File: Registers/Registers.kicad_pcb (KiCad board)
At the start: 2 copper layers, 85 x 99.5 mm, 19 parts

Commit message: Some small Changes
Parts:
- added C1: 100 nF, Capacitor_THT:C_Disc_D5.0mm_W2.5mm_P2.50mm, F.Cu at (92.7, 42.2)
- added C2: 100 nF, Capacitor_THT:C_Disc_D5.0mm_W2.5mm_P2.50mm, F.Cu at (82.8, 118.5)
- added C3: 100 nF, Capacitor_THT:C_Disc_D5.0mm_W2.5mm_P2.50mm, F.Cu at (84.0, 110.0)
- added C4: 100 nF, Capacitor_THT:C_Disc_D5.0mm_W2.5mm_P2.50mm, F.Cu at (45.5, 90.0)
- added J1: Output to Display, Connector_PinHeader_2.54mm:PinHeader_1x04_P2.54mm_Vertical, F.Cu at (68.1, 124.5)
- added J2: Reg Specific Connections, Connector_PinSocket_2.54mm:PinSocket_1x10_P2.54mm_Vertical, F.Cu at (76.0, 45.0)
- added U1: 74HC173, Package_DIP:DIP-16_W7.62mm_Socket_LongPads, F.Cu at (42.4, 81.1)
- added U2: 74HC173, Package_DIP:DIP-16_W7.62mm_Socket_LongPads, F.Cu at (73.9, 81.1)
- added U3: 74HC245, Package_DIP:DIP-20_W7.62mm_Socket_LongPads, F.Cu at (39.9, 63.1)
- added U4: ATtiny84-20P, Package_DIP:DIP-14_W7.62mm, F.Cu at (36.0, 98.5)
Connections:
- B1 pad 10: BUS7 -> BUS0
- B1 pad 11: LBA0 -> LBA7
- B1 pad 12: LBA1 -> LBA6
- B1 pad 13: LBA2 -> LBA5
- B1 pad 14: LBA3 -> LBA4
- B1 pad 15: LBA4 -> LBA3
- B1 pad 16: LBA5 -> LBA2
- B1 pad 17: LBA6 -> LBA1
- B1 pad 18: LBA7 -> LBA0
- B1 pad 19: LBB0 -> LBB7
- B1 pad 20: LBB1 -> LBB6
- B1 pad 21: LBB2 -> LBB5
- B1 pad 22: LBB3 -> LBB4
- B1 pad 23: LBB4 -> LBB3
- B1 pad 24: LBB5 -> LBB2
- B1 pad 25: LBB6 -> LBB1
- B1 pad 26: LBB7 -> LBB0
- B1 pad 3: BUS0 -> BUS7
- B1 pad 4: BUS1 -> BUS6
- B1 pad 5: BUS2 -> BUS5
- B1 pad 6: BUS3 -> BUS4
- B1 pad 7: BUS4 -> BUS3
- B1 pad 8: BUS5 -> BUS2
- B1 pad 9: BUS6 -> BUS1
- B2 pad 10: BUS7 -> BUS0
- B2 pad 3: BUS0 -> BUS7
- B2 pad 4: BUS1 -> BUS6
- B2 pad 5: BUS2 -> BUS5
- B2 pad 6: BUS3 -> BUS4
- B2 pad 7: BUS4 -> BUS3
- B2 pad 8: BUS5 -> BUS2
- B2 pad 9: BUS6 -> BUS1
- D1 pad 2: unconnected-(D1-A-Pad2) -> REG0
- D2 pad 2: unconnected-(D2-A-Pad2) -> REG1
- D3 pad 2: unconnected-(D3-A-Pad2) -> REG2
- D4 pad 2: unconnected-(D4-A-Pad2) -> REG3
- D5 pad 2: unconnected-(D5-A-Pad2) -> REG4
- D6 pad 2: unconnected-(D6-A-Pad2) -> REG5
- D7 pad 2: unconnected-(D7-A-Pad2) -> REG6
- D8 pad 2: unconnected-(D8-A-Pad2) -> REG7
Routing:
- net 5V: track 9.15 -> 43.0 mm
- net CLEAR: track 3.90 -> 35.3 mm, vias 0 -> 1
- net GND: track 45.3 -> 75.9 mm
- net LBB5: track 3.90 -> 16.3 mm
- net LBA5: track 3.90 -> 15.6 mm
- net LBA4: track 3.90 -> 13.5 mm
- net LBB4: track 3.90 -> 13.5 mm
- net CTRL-27: track 4.12 -> 11.7 mm
- net LBB3: track 3.90 -> 8.59 mm
- net LBA3: track 3.90 -> 8.59 mm
- net RAMI: track 3.80 -> 8.06 mm
- net CTRL-31: track 3.80 -> 8.06 mm
- net CTRL-26: track 3.80 -> 8.06 mm
- net CTRL-24: track 3.80 -> 8.06 mm
- net CTRL-19: track 3.80 -> 8.06 mm
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
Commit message: Version of Registers PCB that is before routing.
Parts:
- added J3: LED Wire Bus, Connector_PinSocket_2.54mm:PinSocket_1x08_P2.54mm_Vertical, F.Cu at (76.1, 40.0)
- added J4: LED Wire Bus, Connector_PinSocket_2.54mm:PinSocket_1x08_P2.54mm_Vertical, F.Cu at (84.0, 68.5)
- moved C1 71.0 mm to (38.2, 87.8), turned to 90 degrees
- moved C3 48.8 mm to (51.0, 74.0), turned to 180 degrees
- moved C2 33.3 mm to (71.0, 87.4), turned to 90 degrees
- moved J2 26.6 mm to (67.5, 70.2), turned to 180 degrees
- moved U3 15.7 mm to (54.1, 69.7), turned to 180 degrees
- moved U1 9.57 mm to (45.7, 90.1)
- moved U2 9.10 mm to (75.9, 90.0)
- moved C4 7.62 mm to (44.2, 97.5)
- moved U4 5.43 mm to (39.2, 102.9)
- moved J1 1.62 mm to (68.7, 123.0)
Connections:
- D1 pad 2: REG0 -> Net-(D1-A)
- D2 pad 2: REG1 -> Net-(D2-A)
- D3 pad 2: REG2 -> Net-(D3-A)
- D4 pad 2: REG3 -> Net-(D4-A)
- D5 pad 2: REG4 -> Net-(D5-A)
- D6 pad 2: REG5 -> Net-(D6-A)
- D7 pad 2: REG6 -> Net-(D7-A)
- D8 pad 2: REG7 -> Net-(D8-A)
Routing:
- net 5V: track 43.0 -> 9.15 mm
- net CLEAR: track 35.3 -> 3.90 mm, vias 1 -> 0
- net GND: track 75.9 -> 45.3 mm
- net LBB5: track 16.3 -> 3.90 mm
- net LBA5: track 15.6 -> 3.90 mm
- net LBA4: track 13.5 -> 3.90 mm
- net LBB4: track 13.5 -> 3.90 mm
- net CTRL-27: track 11.7 -> 4.12 mm
- net LBB3: track 8.59 -> 3.90 mm
- net LBA3: track 8.59 -> 3.90 mm
- net RAMI: track 8.06 -> 3.80 mm
- net CTRL-31: track 8.06 -> 3.80 mm
- net CTRL-26: track 8.06 -> 3.80 mm
- net CTRL-24: track 8.06 -> 3.80 mm
- net CTRL-19: track 8.06 -> 3.80 mm
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
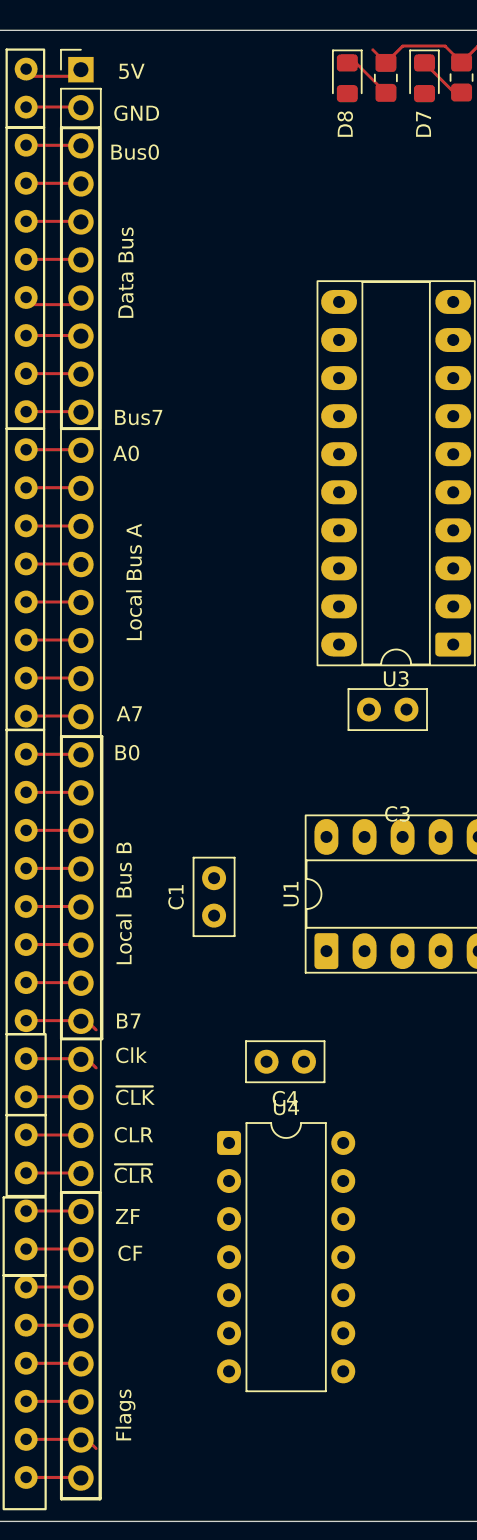
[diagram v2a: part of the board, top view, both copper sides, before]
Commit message: Fixed some issues with the orientation of the local buses on the side-rails.
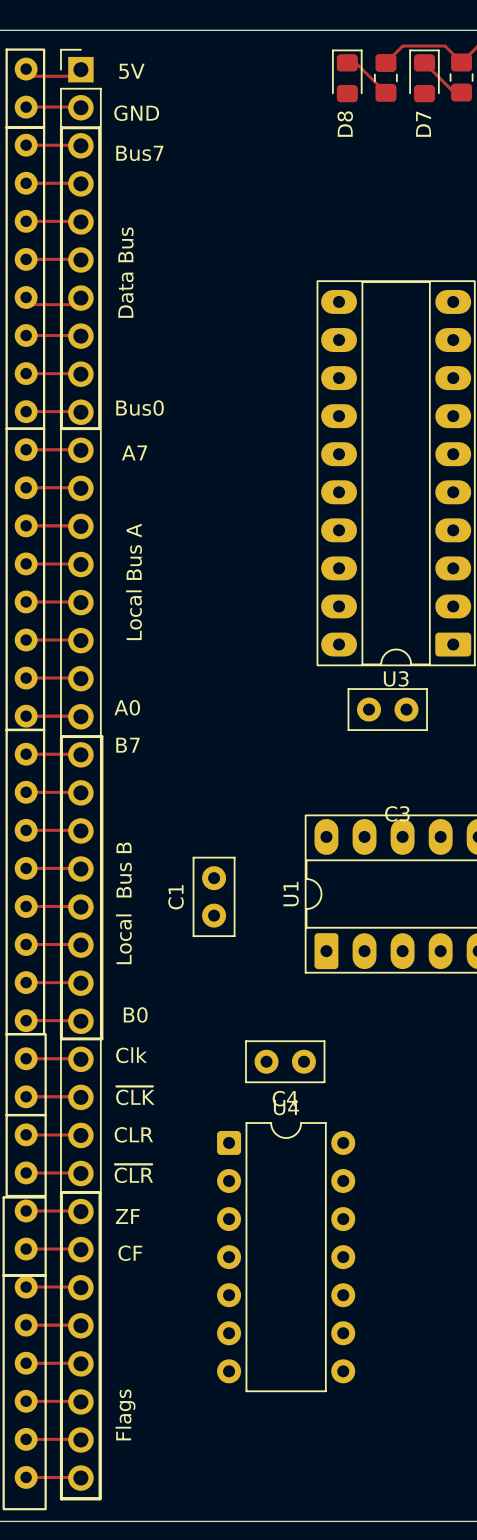
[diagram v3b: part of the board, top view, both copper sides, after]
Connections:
- B2 pad 11: LBA0 -> LBA7
- B2 pad 12: LBA1 -> LBA6
- B2 pad 13: LBA2 -> LBA5
- B2 pad 14: LBA3 -> LBA4
- B2 pad 15: LBA4 -> LBA3
- B2 pad 16: LBA5 -> LBA2
- B2 pad 17: LBA6 -> LBA1
- B2 pad 18: LBA7 -> LBA0
- B2 pad 19: LBB0 -> LBB7
- B2 pad 20: LBB1 -> LBB6
- B2 pad 21: LBB2 -> LBB5
- B2 pad 22: LBB3 -> LBB4
- B2 pad 23: LBB4 -> LBB3
- B2 pad 24: LBB5 -> LBB2
- B2 pad 25: LBB6 -> LBB1
- B2 pad 26: LBB7 -> LBB0
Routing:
- net GND: track 45.3 -> 44.0 mm

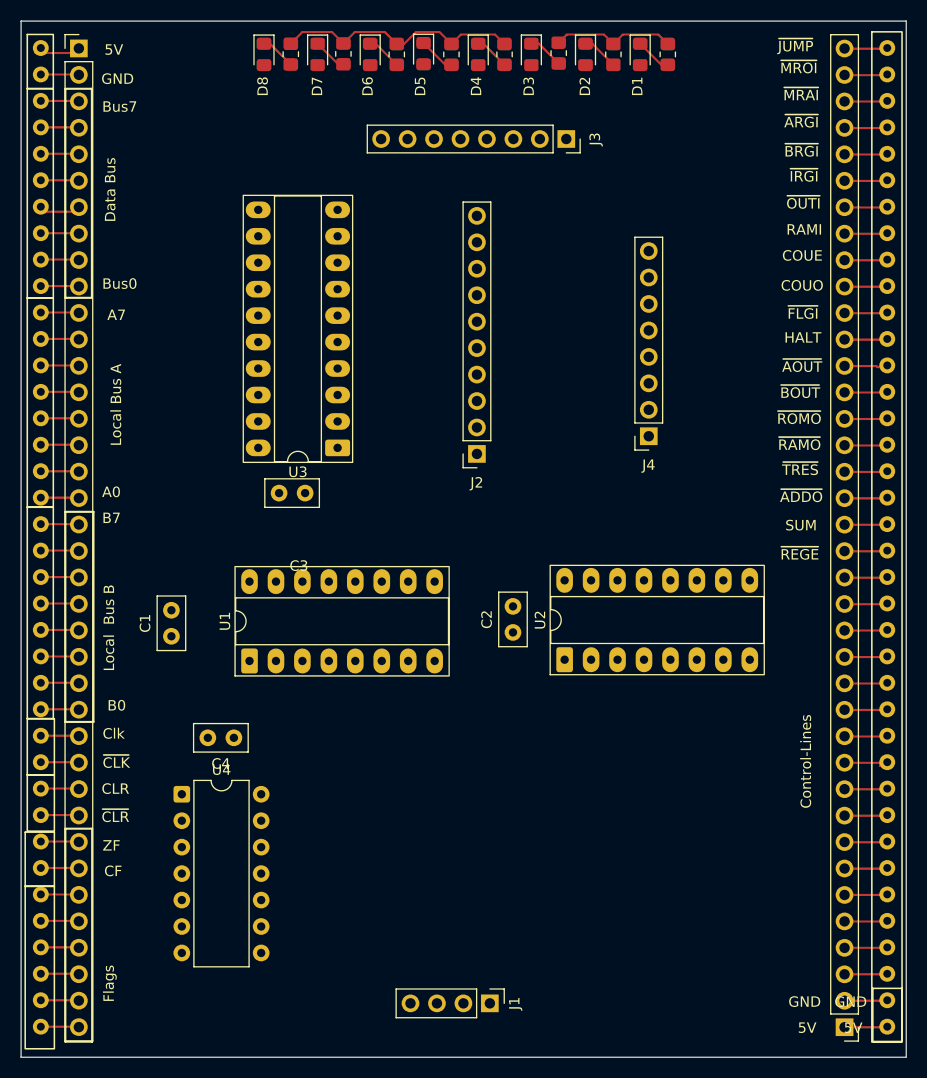
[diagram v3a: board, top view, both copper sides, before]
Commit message: Split 5V pins into different nets
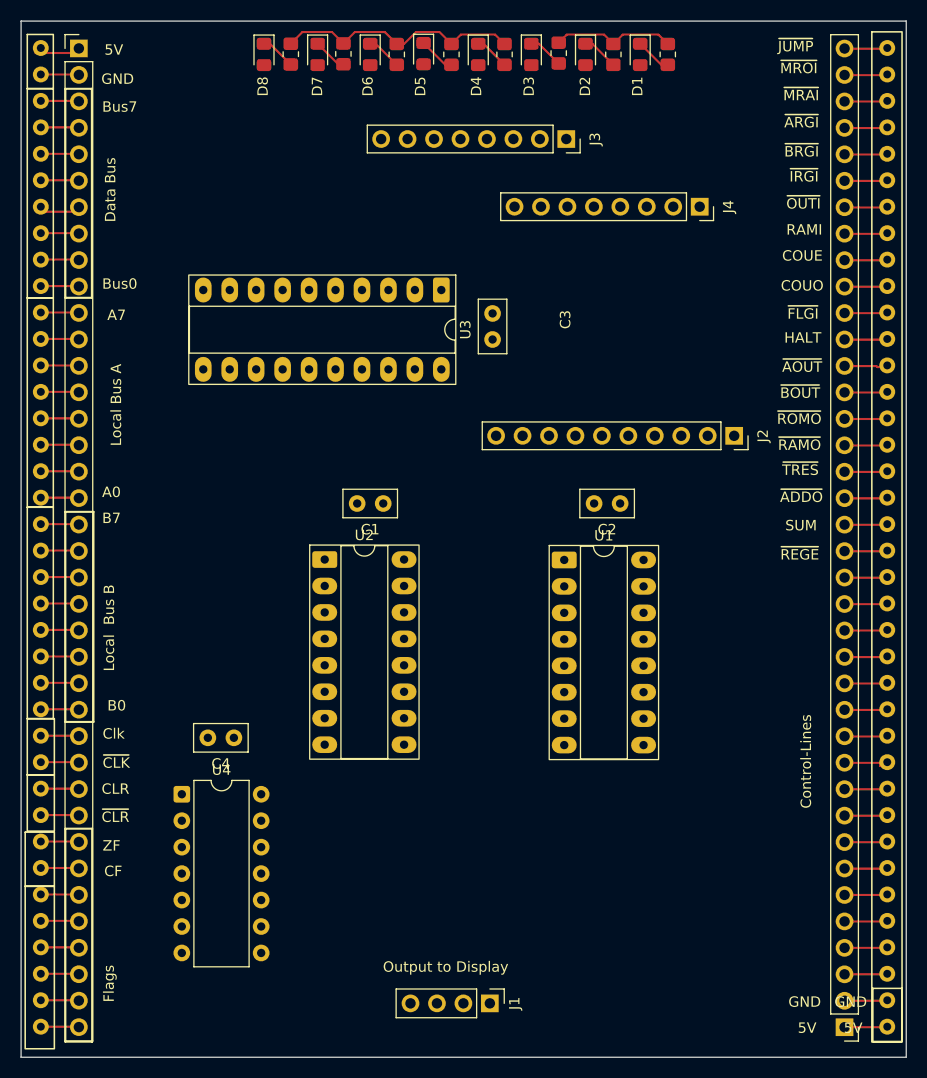
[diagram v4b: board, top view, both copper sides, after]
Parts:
- moved U1 31.7 mm to (75.9, 80.4), turned to 0 degrees
- moved U2 25.0 mm to (52.9, 80.4), turned to 0 degrees
- moved C3 24.9 mm to (69.0, 56.8), turned to -90 degrees
- moved J2 24.8 mm to (92.2, 68.5), turned to -90 degrees
- moved C1 24.0 mm to (58.5, 75.0), turned to 180 degrees
- moved J4 22.6 mm to (88.9, 46.5), turned to -90 degrees
- moved U3 18.1 mm to (64.1, 54.5), turned to -90 degrees
- moved C2 16.1 mm to (81.2, 75.0), turned to 180 degrees
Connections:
- B3 pad 1: 5V -> 5V_2
- C4 pad 2: 5V -> 5V_2
- J1 pad 1: 5V -> 5V_2
- U4 pad 1: 5V -> 5V_2

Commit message: First version of Registers
Routing done for PCB
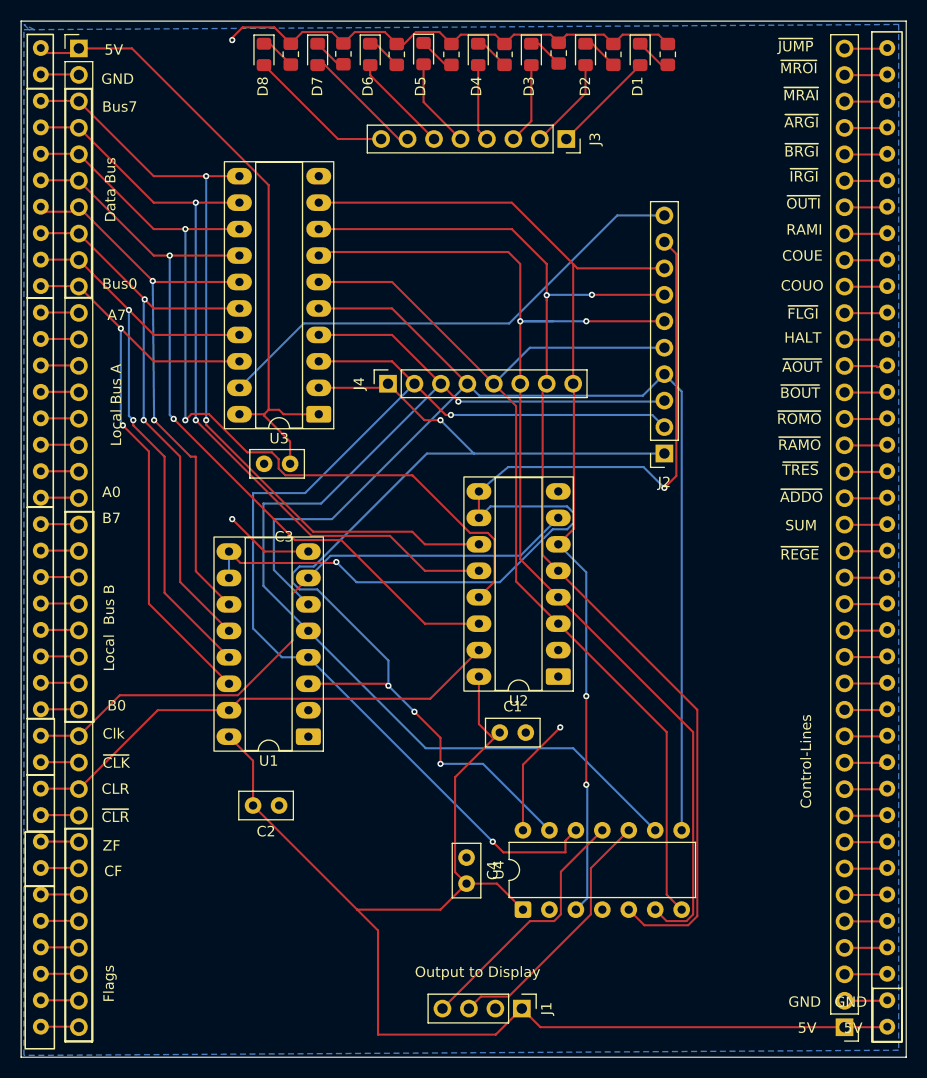
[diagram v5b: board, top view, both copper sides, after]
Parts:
- moved C2 43.7 mm to (48.5, 104.0)
- moved U4 34.6 mm to (71.9, 114.0), turned to 90 degrees
- moved J4 34.4 mm to (59.0, 63.5), turned to 90 degrees
- moved U1 29.9 mm to (51.3, 97.4), turned to 180 degrees
- moved C4 25.1 mm to (66.5, 109.0), turned to -90 degrees
- moved U2 25.1 mm to (75.3, 91.6), turned to 180 degrees
- moved C1 24.7 mm to (69.7, 97.0), turned to 0 degrees
- moved C3 24.2 mm to (49.6, 71.2), turned to 180 degrees
- moved U3 16.8 mm to (52.3, 66.4), turned to 180 degrees
- moved J2 6.91 mm to (85.5, 70.2), turned to 180 degrees
- moved J1 3.11 mm to (71.8, 123.5)
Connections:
- B1 pad 39: 5V -> 5V_2
- C1 pad 1: 5V -> 5V_2
- C2 pad 2: 5V -> 5V_2
- U1 pad 16: 5V -> 5V_2
- U2 pad 16: 5V -> 5V_2
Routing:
- net 5V_2: track 0.00 -> 126.5 mm
- net REG3: track 0.00 -> 115.5 mm
- net REG2: track 0.00 -> 113.0 mm, vias 0 -> 1
- net REG6: track 0.00 -> 111.6 mm, vias 0 -> 2
- net REG5: track 0.00 -> 110.6 mm, vias 0 -> 2
- net REG1: track 0.00 -> 110.1 mm, vias 0 -> 2
- net REG0: track 0.00 -> 103.8 mm, vias 0 -> 4
- net REG7: track 0.00 -> 100.1 mm, vias 0 -> 2
- net ~{RIN}: track 0.00 -> 96.7 mm, vias 0 -> 2
- net REG4: track 0.00 -> 96.6 mm
- net BUS5: track 3.90 -> 82.3 mm, vias 0 -> 2
- net BUS7: track 3.90 -> 77.1 mm, vias 0 -> 2
- net BUS6: track 3.90 -> 76.4 mm, vias 0 -> 2
- net BUS4: track 3.90 -> 76.0 mm, vias 0 -> 2
- net CLOCK: track 3.90 -> 61.3 mm
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- added copper zone on B.Cu, net GND

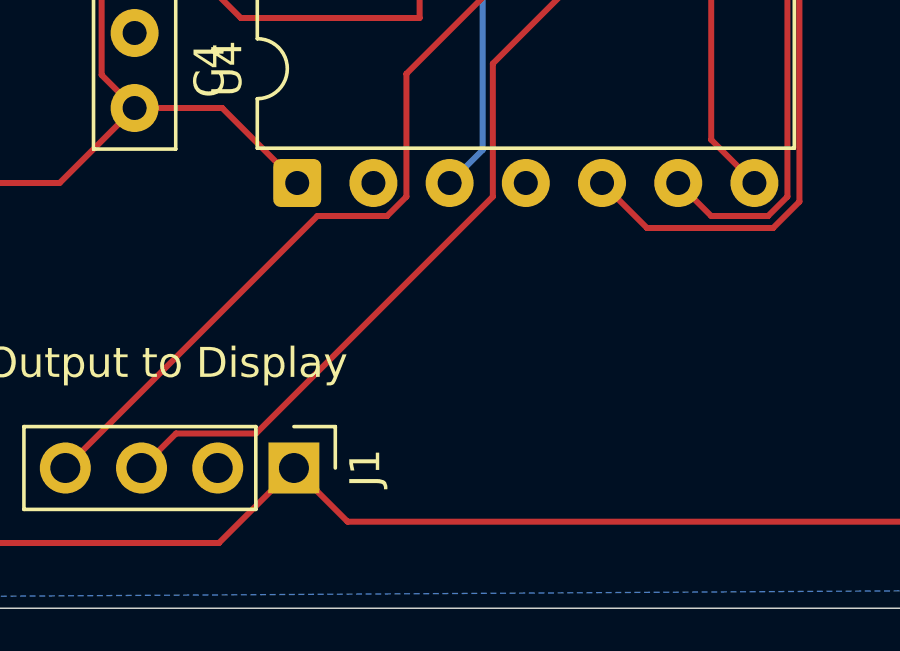
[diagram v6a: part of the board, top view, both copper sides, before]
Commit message: Added pull up resistor for ATTtiny84 Reset Pin
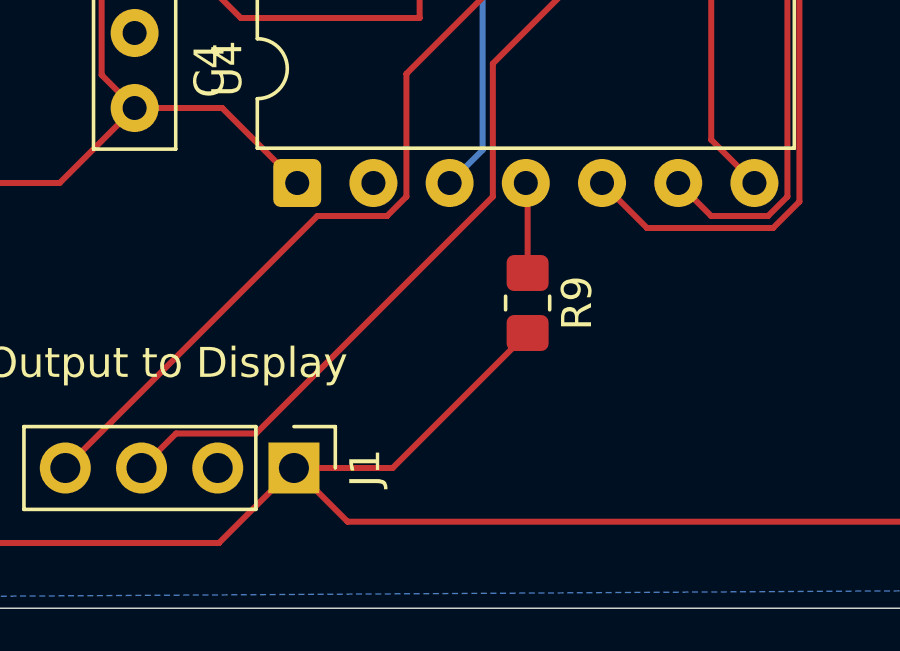
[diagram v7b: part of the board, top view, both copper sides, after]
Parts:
- added R9: 4.7K, Resistor_SMD:R_0805_2012Metric_Pad1.20x1.40mm_HandSolder, F.Cu at (79.6, 118.0)
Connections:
- U4 pad 4: unconnected-(U4-~{RESET}/PB3-Pad4) -> Net-(U4-~{RESET}/PB3)
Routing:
- net 5V_2: track 126.5 -> 136.2 mm
- net Net-(U4-~{RESET}/PB3): track 0.00 -> 3.02 mm
